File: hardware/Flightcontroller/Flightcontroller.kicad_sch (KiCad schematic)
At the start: 0 parts

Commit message: add components to kicad
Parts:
- added U1: STM32F765VGT6, easyeda2kicad:LQFP-100_L14.0-W14.0-P0.50-LS16.0-BL, symbol easyeda2kicad:STM32F765VGT6
- added U2: ICM-45686, easyeda2kicad:LGA-14_L3.0-W2.5-P0.50-TL, symbol easyeda2kicad:ICM-45686
- added U3: BMP580, easyeda2kicad:LGA-10_L2.0-W2.0-P0.50-TL_BMP580, symbol easyeda2kicad:BMP580
- added U4: TPS63070RNMR, easyeda2kicad:VQFN-15_L3.0-W2.5-P0.50-BL, symbol easyeda2kicad:TPS63070RNMR
- added U5: LMR51430YFDDCR, easyeda2kicad:SOT-23-6_L2.9-W1.6-P0.95-LS2.9-BL, symbol easyeda2kicad:LMR51430YFDDCR

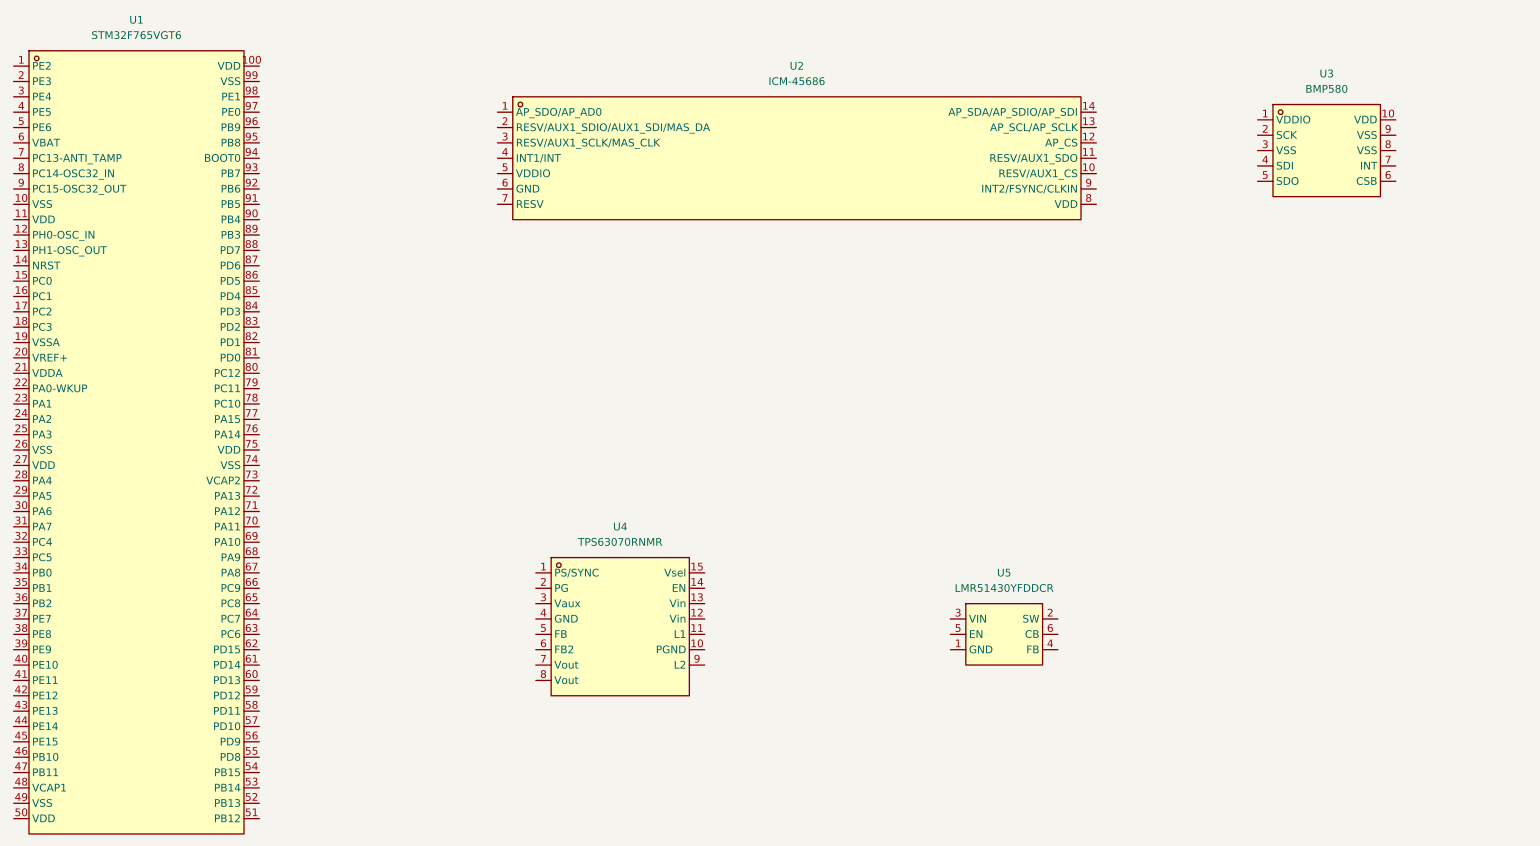
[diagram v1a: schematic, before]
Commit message: imu wired
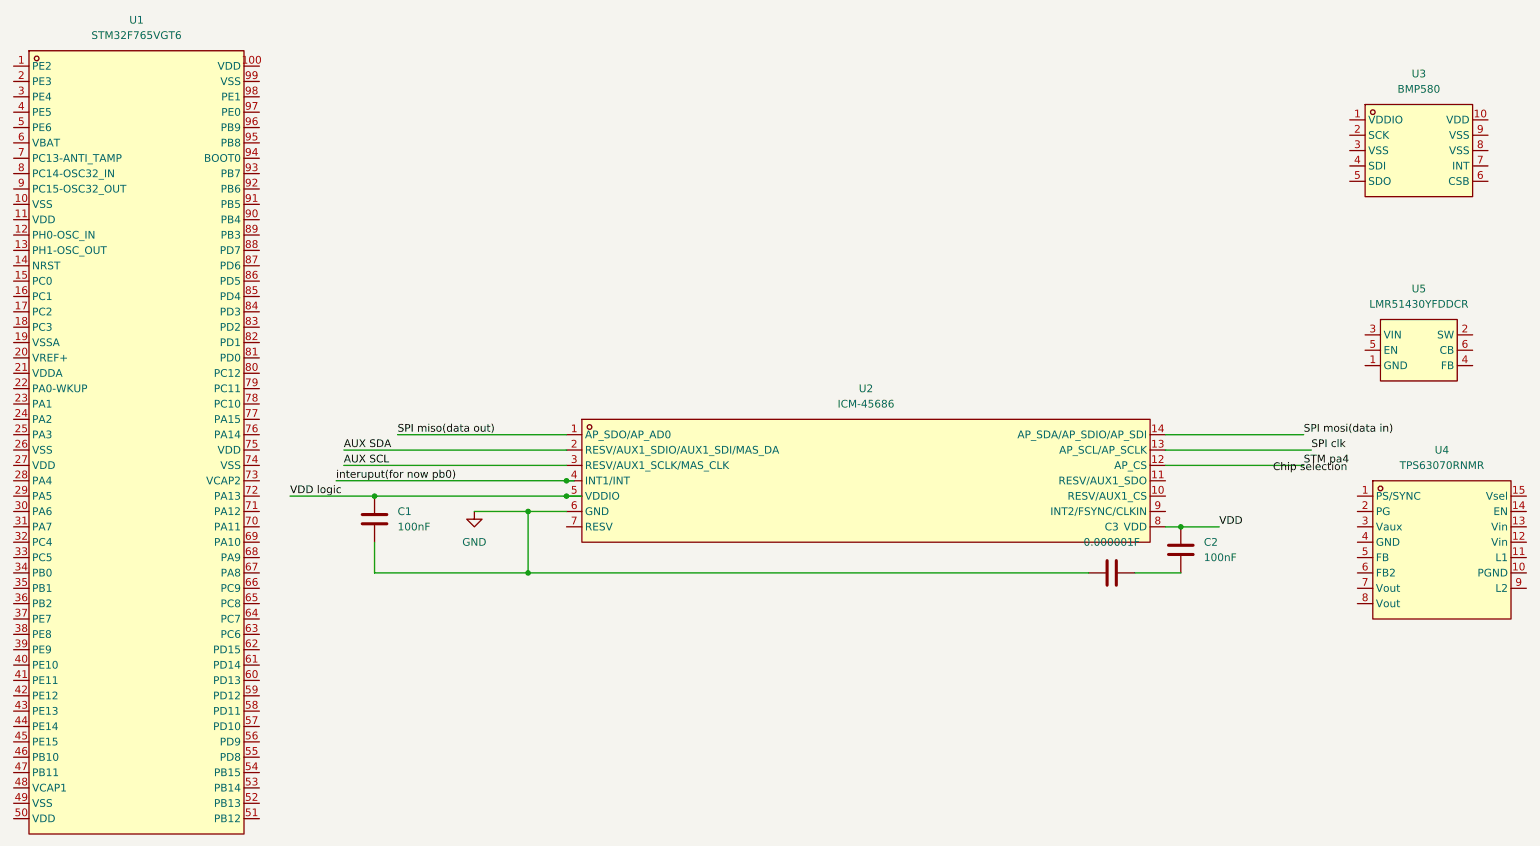
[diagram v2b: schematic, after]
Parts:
- added C1, C2: 100nF, symbol Device:C
- added C3: 0.000001F, symbol Device:C
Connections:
- net SPI miso(data out): now reaches U2.1 (AP_SDO/AP_AD0)
- net STM pa4: now reaches U2.12 (AP_CS)
- net SPI clk: now reaches U2.13 (AP_SCL/AP_SCLK)
- net SPI mosi(data in): now reaches U2.14 (AP_SDA/AP_SDIO/AP_SDI)
- net AUX SDA: now reaches U2.2 (RESV/AUX1_SDIO/AUX1_SDI/MAS_DA)
- net AUX SCL: now reaches U2.3 (RESV/AUX1_SCLK/MAS_CLK)
- net interuput(for now pb0): now reaches U2.4 (INT1/INT)
- net VDD logic: now reaches U2.5 (VDDIO)
- net VDD logic: now also C1.1
- net GND: now reaches U2.6 (GND)
- net GND: now also C1.2, C3.2
- net VDD: now reaches U2.8 (VDD)
- net VDD: now also C2.1
- new net: C2.2, C3.1
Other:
- moved on the sheet: U2, U3, U4, U5
